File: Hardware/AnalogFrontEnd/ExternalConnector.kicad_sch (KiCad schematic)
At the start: 0 parts

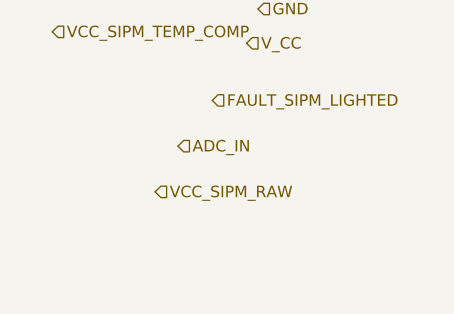
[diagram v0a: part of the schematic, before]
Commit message: add bias supply circuit
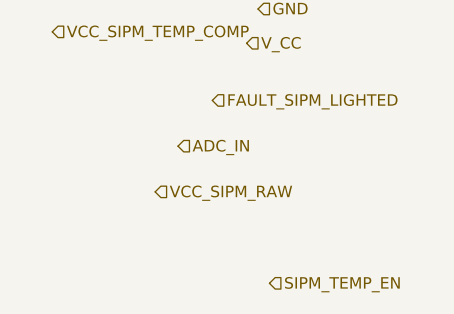
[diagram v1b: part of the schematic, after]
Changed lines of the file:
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@@
+		)
+	)
+	(hierarchical_label "SIPM_TEMP_EN"
+		(shape input)
+		(at 67.31 109.22 0)
+		(effects
+			(font
+				(size 1.27 1.27)
+			)
+			(justify left)
 		)
 	)

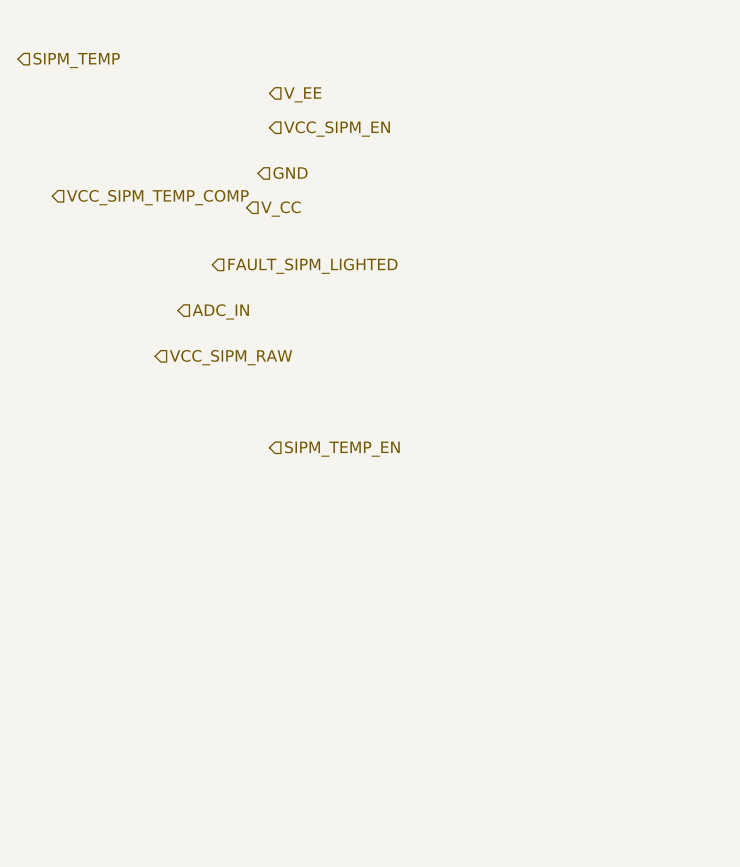
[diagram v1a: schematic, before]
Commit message: add draft of data processing circuit
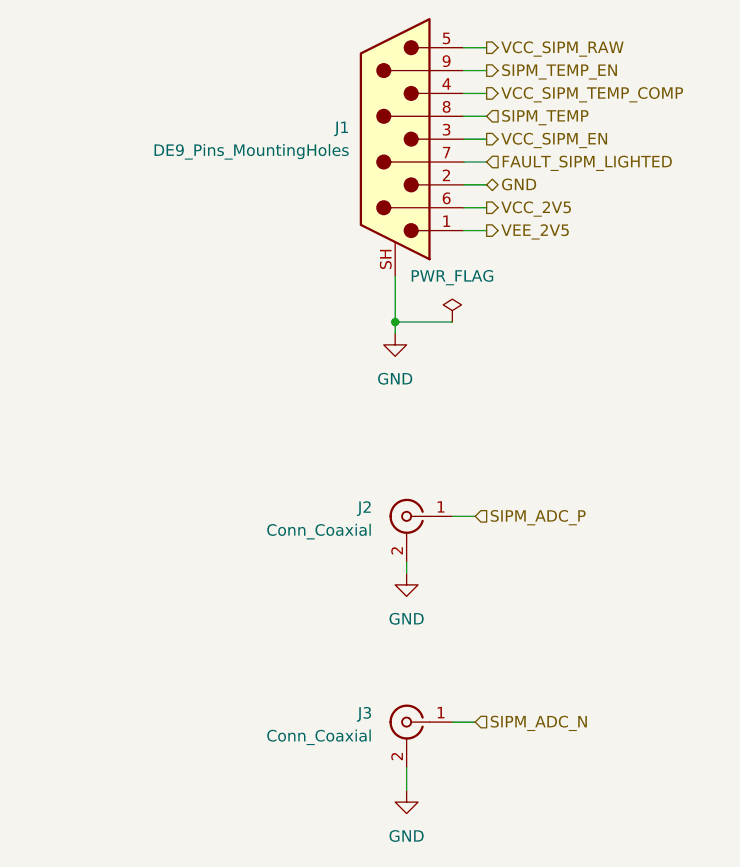
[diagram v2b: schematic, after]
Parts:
- added J1: DE9_Pins_MountingHoles, Connector_Dsub:DSUB-9_Socket_Vertical_P2.77x2.84mm_MountingHoles, symbol Connector:DE9_Pins_MountingHoles
- added J2, J3: Conn_Coaxial, symbol Connector:Conn_Coaxial
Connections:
- net FAULT_SIPM_LIGHTED: now also J1.7
- net GND: now also J1.2, J1.SH (PAD), J2.2 (Ext), J3.2 (Ext)
- net SIPM_TEMP: now also J1.8
- net SIPM_TEMP_EN: now also J1.9
- net VCC_SIPM_EN: now also J1.3
- net VCC_SIPM_RAW: now also J1.5
- net VCC_SIPM_TEMP_COMP: now also J1.4
- new net SIPM_ADC_N: J3.1 (In)
- new net SIPM_ADC_P: J2.1 (In)
- new net VCC_2V5: J1.6
- new net VEE_2V5: J1.1
